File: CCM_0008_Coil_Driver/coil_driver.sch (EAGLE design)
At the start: 203 parts, among them IC1 AD8675, IC10 AD8675, IC11 AD825, IC12 AD825, IC13 AD825, IC14 AD825, IC15 AD825, IC16 AD825, IC17 BUF634U, IC2 AD797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

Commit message: Added CAD and docs for CCM_0008
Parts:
- C2, C4: value 0.1uF -> 0.1u
- C22, C72: value 100nF -> 0.1u
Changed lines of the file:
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@@
 <setting verticaltext="up"/>
 </settings>
-<grid distance="0.025" unitdist="inch" unit="inch" style="lines" multiple="1" display="yes" altdistance="0.01" altunitdist="inch" altunit="inch"/>
+<grid distance="0.1" unitdist="inch" unit="inch" style="lines" multiple="1" display="no" altdistance="0.01" altunitdist="inch" altunit="inch"/>
 <layers>
 <layer number="1" name="Top" color="4" fill="1" visible="no" active="no"/>
@@
 <part name="R9" library="Fitch" deviceset="TRIM_US-" device="B90P" value="20k"/>
 <part name="SUPPLY3" library="supply2" deviceset="GND" device=""/>
-<part name="C2" library="acrooptics" deviceset="C" device="0603" value="0.1uF"/>
+<part name="C2" library="acrooptics" deviceset="C" device="0603" value="0.1u"/>
 <part name="IC14" library="noah" deviceset="AD825_A" device="" value="AD825"/>
 <part name="P-14" library="supply1" deviceset="-15V" device=""/>
@@
 <part name="R53" library="Fitch" deviceset="TRIM_US-" device="B90P" value="20k"/>
 <part name="SUPPLY5" library="supply2" deviceset="GND" device=""/>
-<part name="C4" library="acrooptics" deviceset="C" device="0603" value="0.1uF"/>
+<part name="C4" library="acrooptics" deviceset="C" device="0603" value="0.1u"/>
 <part name="IC15" library="noah" deviceset="AD825_A" device="" value="AD825"/>
 <part name="P-17" library="supply1" deviceset="-15V" device=""/>
@@
 <part name="SUPPLY28" library="supply2" deviceset="GND" device=""/>
 <part name="S1" library="noah" deviceset="71BDF30" device=""/>
-<part name="C72" library="acrooptics" deviceset="C" device="0603" value="100nF"/>
+<part name="C72" library="acrooptics" deviceset="C" device="0603" value="0.1u"/>
 <part name="C73" library="acrooptics" deviceset="C" device="0603" value="47nF"/>
 <part name="C74" library="acrooptics" deviceset="C" device="0603" value="22nF"/>
@@
 <part name="C82" library="acrooptics" deviceset="C" device="0603" value="47pF"/>
 <part name="S2" library="noah" deviceset="71BDF30" device=""/>
-<part name="C22" library="acrooptics" deviceset="C" device="0603" value="100nF"/>
+<part name="C22" library="acrooptics" deviceset="C" device="0603" value="0.1u"/>
 <part name="C71" library="acrooptics" deviceset="C" device="0603" value="47nF"/>
 <part name="C83" library="acrooptics" deviceset="C" device="0603" value="22nF"/>

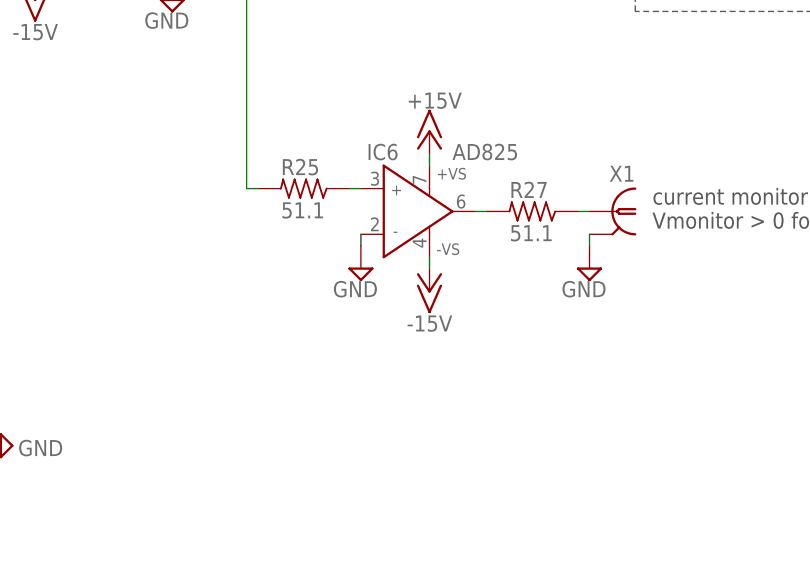
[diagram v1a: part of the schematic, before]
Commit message: CCM_0008: fixed current monitor schematic wiring error, prototype run current-monitor output will rail if not fixed in hardware.
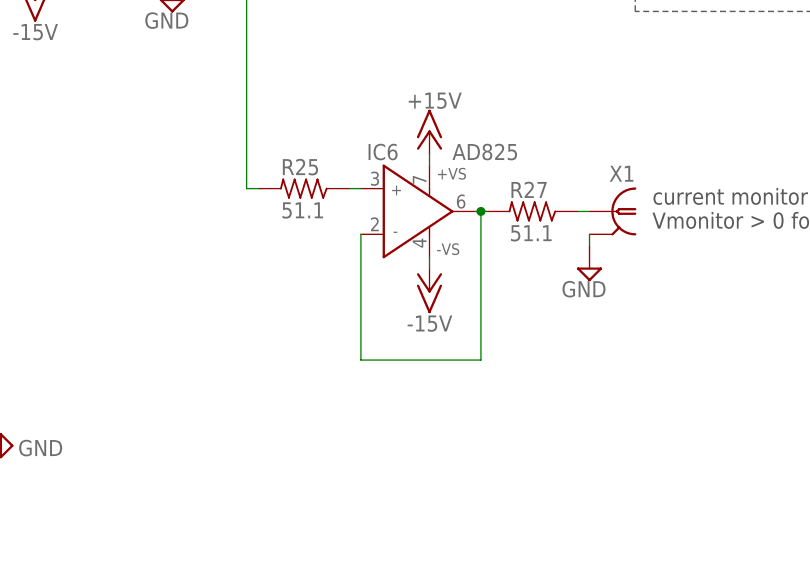
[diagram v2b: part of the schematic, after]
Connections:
- removed net N$24: IC6.OUT, R27.2
- new net N$6: IC6.IN-, IC6.OUT, R27.2
- net GND: no longer IC6.IN-
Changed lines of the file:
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@@
 <setting verticaltext="up"/>
 </settings>
-<grid distance="0.1" unitdist="inch" unit="inch" style="lines" multiple="1" display="no" altdistance="0.01" altunitdist="inch" altunit="inch"/>
+<grid distance="0.025" unitdist="inch" unit="inch" style="lines" multiple="1" display="no" altdistance="0.01" altunitdist="inch" altunit="inch"/>
 <layers>
 <layer number="1" name="Top" color="4" fill="1" visible="no" active="no"/>
@@
 <part name="P-3" library="supply1" deviceset="-15V" device=""/>
 <part name="P+6" library="supply1" deviceset="+15V" device=""/>
-<part name="SUPPLY17" library="supply2" deviceset="GND" device=""/>
 <part name="R27" library="acrooptics" deviceset="R" device="0603" value="51.1"/>
 <part name="P+7" library="supply1" deviceset="+15V" device=""/>
@@
 <attribute name="VALUE" x="103.505" y="78.105" size="1.778" layer="96"/>
 </instance>
-<instance part="SUPPLY17" gate="GND" x="142.24" y="17.78" smashed="yes" rot="MR0">
-<attribute name="VALUE" x="144.145" y="14.605" size="1.778" layer="96" rot="MR0"/>
-</instance>
 <instance part="R27" gate="R$1" x="161.29" y="24.13" smashed="yes" rot="R180">
 <attribute name="NAME" x="158.75" y="25.6286" size="1.778" layer="95"/>
@@
 </segment>
 <segment>
-<pinref part="SUPPLY17" gate="GND" pin="GND"/>
-<wire x1="142.24" y1="21.59" x2="142.24" y2="20.32" width="0.1524" layer="91"/>
-<pinref part="IC6" gate="P" pin="IN-"/>
-</segment>
-<segment>
 <pinref part="X1" gate="G$1" pin="2"/>
 <pinref part="SUPPLY18" gate="GND" pin="GND"/>
@@
 </segment>
 </net>
-<net name="N$24" class="0">
-<segment>
-<wire x1="154.94" y1="24.13" x2="156.21" y2="24.13" width="0.1524" layer="91"/>
-<pinref part="R27" gate="R$1" pin="2"/>
-<pinref part="IC6" gate="P" pin="OUT"/>
-</segment>
-</net>
 <net name="N$25" class="0">
 <segment>
@@
 </segment>
 </net>
+<net name="N$6" class="0">
+<segment>
+<pinref part="IC6" gate="P" pin="IN-"/>
+<wire x1="142.24" y1="21.59" x2="142.24" y2="7.62" width="0.1524" layer="91"/>
+<wire x1="154.94" y1="24.13" x2="155.575" y2="24.13" width="0.1524" layer="91"/>
+<pinref part="R27" gate="R$1" pin="2"/>
+<pinref part="IC6" gate="P" pin="OUT"/>
+<wire x1="155.575" y1="24.13" x2="156.21" y2="24.13" width="0.1524" layer="91"/>
+<wire x1="142.24" y1="7.62" x2="155.575" y2="7.62" width="0.1524" layer="91"/>
+<wire x1="155.575" y1="7.62" x2="155.575" y2="24.13" width="0.1524" layer="91"/>
+<junction x="155.575" y="24.13"/>
+</segment>
+</net>
